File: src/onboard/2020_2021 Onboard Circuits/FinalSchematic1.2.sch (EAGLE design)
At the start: 79 parts, among them IC1 MIC2937A-5.0BT, IC3 A5975D

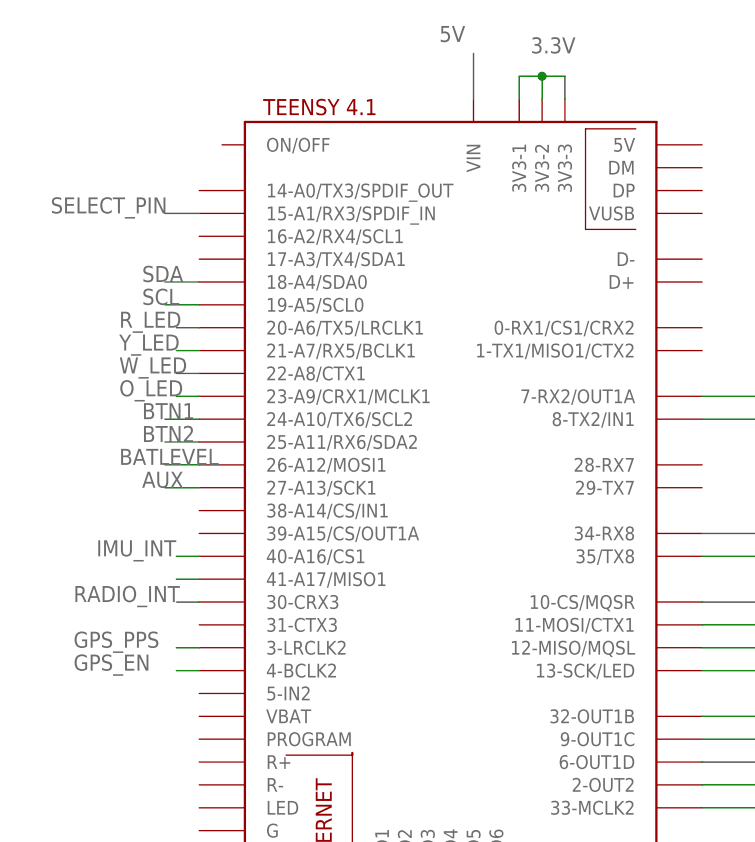
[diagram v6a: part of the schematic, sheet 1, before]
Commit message: Formatting changes and 6v test point
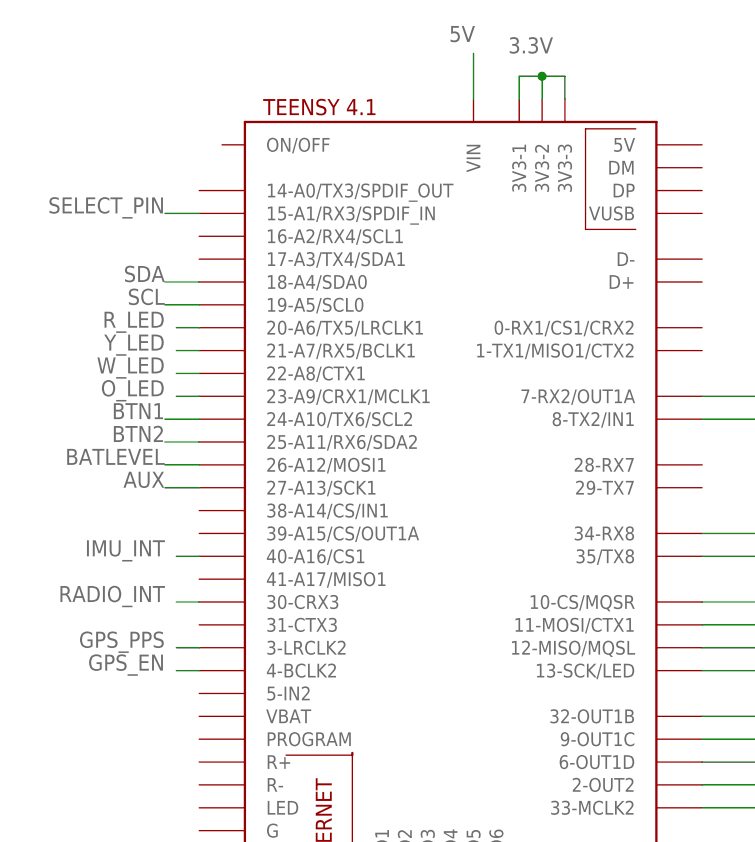
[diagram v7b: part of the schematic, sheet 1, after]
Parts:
- renumbered JUMPER_TO_NAV to NAV
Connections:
- removed net MISO1: TEENSY4.1.41-A17/MISO1
- removed net N$5: TP5.TP
- net 6V: now also TP5.TP
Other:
- note added: "I2C pull-up resistors"
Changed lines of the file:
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@@
 <part name="GND6" library="supply1" library_urn="urn:adsk.eagle:library:371" deviceset="GND" device=""/>
 <part name="L2" library="rcl" library_urn="urn:adsk.eagle:library:334" deviceset="L-US" device="TFI0307" package3d_urn="urn:adsk.eagle:package:23534/1" value="27uH"/>
-<part name="JUMPER_TO_NAV" library="pinhead" library_urn="urn:adsk.eagle:library:325" deviceset="PINHD-1X4" device="" package3d_urn="urn:adsk.eagle:package:22407/2"/>
+<part name="NAV" library="pinhead" library_urn="urn:adsk.eagle:library:325" deviceset="PINHD-1X4" device="" package3d_urn="urn:adsk.eagle:package:22407/2"/>
 <part name="ORANGE" library="adafruit" library_urn="urn:adsk.eagle:library:420" deviceset="R-US_" device="0204/7" package3d_urn="urn:adsk.eagle:package:6240596/1" value="150"/>
 <part name="C3" library="capacitor-wima" library_urn="urn:adsk.eagle:library:116" deviceset="C" device="2,5-3" package3d_urn="urn:adsk.eagle:package:5436/1" value="10uF"/>
@@
 <part name="AUX" library="pinhead" library_urn="urn:adsk.eagle:library:325" deviceset="PINHD-1X3" device="" package3d_urn="urn:adsk.eagle:package:22458/2"/>
 <part name="GND12" library="supply1" library_urn="urn:adsk.eagle:library:371" deviceset="GND" device=""/>
+<part name="GND15" library="supply1" library_urn="urn:adsk.eagle:library:371" deviceset="GND" device=""/>
 </parts>
 <sheets>
@@
 <pinref part="TEENSY4.1" gate="G$1" pin="VIN"/>
 <wire x1="64.77" y1="91.44" x2="64.77" y2="96.52" width="0.1524" layer="91"/>
-<label x="60.96" y="97.79" size="1.778" layer="95"/>
+<label x="63.5" y="97.79" size="1.778" layer="95" align="bottom-center"/>
 </segment>
 </net>
@@
 <wire x1="74.93" y1="93.98" x2="72.39" y2="93.98" width="0.1524" layer="91"/>
 <junction x="72.39" y="93.98"/>
-<label x="71.12" y="96.52" size="1.778" layer="95"/>
+<label x="71.12" y="96.52" size="1.778" layer="95" align="bottom-center"/>
 </segment>
 </net>
@@
 <pinref part="TEENSY4.1" gate="G$1" pin="18-A4/SDA0"/>
 <wire x1="34.29" y1="71.12" x2="30.48" y2="71.12" width="0.1524" layer="91"/>
-<label x="27.94" y="71.12" size="1.778" layer="95"/>
+<label x="30.48" y="71.12" size="1.778" layer="95" align="bottom-right"/>
 </segment>
 </net>
@@
 <pinref part="TEENSY4.1" gate="G$1" pin="19-A5/SCL0"/>
 <wire x1="34.29" y1="68.58" x2="30.48" y2="68.58" width="0.1524" layer="91"/>
-<label x="27.94" y="68.58" size="1.778" layer="95"/>
-</segment>
-</net>
-<net name="MISO1" class="0">
-<segment>
-<pinref part="TEENSY4.1" gate="G$1" pin="41-A17/MISO1"/>
-<wire x1="34.29" y1="38.1" x2="31.75" y2="38.1" width="0.1524" layer="91"/>
+<label x="30.48" y="68.58" size="1.778" layer="95" align="bottom-right"/>
 </segment>
 </net>
@@
 <pinref part="TEENSY4.1" gate="G$1" pin="4-BCLK2"/>
 <wire x1="34.29" y1="27.94" x2="31.75" y2="27.94" width="0.1524" layer="91"/>
-<label x="20.32" y="27.94" size="1.778" layer="95"/>
+<label x="30.48" y="27.94" size="1.778" layer="95" align="bottom-right"/>
 </segment>
 </net>
@@
 <pinref part="TEENSY4.1" gate="G$1" pin="3-LRCLK2"/>
 <wire x1="34.29" y1="30.48" x2="31.75" y2="30.48" width="0.1524" layer="91"/>
-<label x="20.32" y="30.48" size="1.778" layer="95"/>
+<label x="30.48" y="30.48" size="1.778" layer="95" align="bottom-right"/>
 </segment>
 </net>
@@
 <pinref part="TEENSY4.1" gate="G$1" pin="30-CRX3"/>
 <wire x1="34.29" y1="35.56" x2="31.75" y2="35.56" width="0.1524" layer="91"/>
-<label x="20.32" y="35.56" size="1.778" layer="95"/>
+<label x="30.48" y="35.56" size="1.778" layer="95" align="bottom-right"/>
 </segment>
 </net>
@@
 <pinref part="TEENSY4.1" gate="G$1" pin="40-A16/CS1"/>
 <wire x1="34.29" y1="40.64" x2="31.75" y2="40.64" width="0.1524" layer="91"/>
-<label x="22.86" y="40.64" size="1.778" layer="95"/>
+<label x="30.48" y="40.64" size="1.778" layer="95" align="bottom-right"/>
 </segment>
 </net>
@@
 <pinref part="TEENSY4.1" gate="G$1" pin="22-A8/CTX1"/>
 <wire x1="34.29" y1="60.96" x2="31.75" y2="60.96" width="0.1524" layer="91"/>
-<label x="25.4" y="60.96" size="1.778" layer="95"/>
+<label x="30.48" y="60.96" size="1.778" layer="95" align="bottom-right"/>
 </segment>
 </net>
@@
 <pinref part="TEENSY4.1" gate="G$1" pin="21-A7/RX5/BCLK1"/>
 <wire x1="34.29" y1="63.5" x2="31.75" y2="63.5" width="0.1524" layer="91"/>
-<label x="25.4" y="63.5" size="1.778" layer="95"/>
+<label x="30.48" y="63.5" size="1.778" layer="95" align="bottom-right"/>
 </segment>
 </net>
@@
 <pinref part="TEENSY4.1" gate="G$1" pin="20-A6/TX5/LRCLK1"/>
 <wire x1="34.29" y1="66.04" x2="31.75" y2="66.04" width="0.1524" layer="91"/>
-<label x="25.4" y="66.04" size="1.778" layer="95"/>
+<label x="30.48" y="66.04" size="1.778" layer="95" align="bottom-right"/>
 </segment>
 </net>
@@
 <pinref part="TEENSY4.1" gate="G$1" pin="15-A1/RX3/SPDIF_IN"/>
 <wire x1="34.29" y1="78.74" x2="30.48" y2="78.74" width="0.1524" layer="91"/>
-<label x="17.78" y="78.74" size="1.778" layer="95"/>
+<label x="30.48" y="78.74" size="1.778" layer="95" align="bottom-right"/>
 </segment>
 </net>
@@
 <pinref part="TEENSY4.1" gate="G$1" pin="23-A9/CRX1/MCLK1"/>
 <wire x1="34.29" y1="58.42" x2="31.75" y2="58.42" width="0.1524" layer="91"/>
-<label x="25.4" y="58.42" size="1.778" layer="95"/>
+<label x="30.48" y="58.42" size="1.778" layer="95" align="bottom-right"/>
 </segment>
 </net>
@@
 <pinref part="TEENSY4.1" gate="G$1" pin="25-A11/RX6/SDA2"/>
 <wire x1="34.29" y1="53.34" x2="30.48" y2="53.34" width="0.1524" layer="91"/>
-<label x="27.94" y="53.34" size="1.778" layer="95"/>
+<label x="30.48" y="53.34" size="1.778" layer="95" align="bottom-right"/>
 </segment>
 </net>
@@
 <pinref part="TEENSY4.1" gate="G$1" pin="24-A10/TX6/SCL2"/>
 <wire x1="34.29" y1="55.88" x2="30.48" y2="55.88" width="0.1524" layer="91"/>
-<label x="27.94" y="55.88" size="1.778" layer="95"/>
+<label x="30.48" y="55.88" size="1.778" layer="95" align="bottom-right"/>
 </segment>
 </net>
@@
 <pinref part="TEENSY4.1" gate="G$1" pin="26-A12/MOSI1"/>
 <wire x1="34.29" y1="50.8" x2="30.48" y2="50.8" width="0.1524" layer="91"/>
-<label x="25.4" y="50.8" size="1.778" layer="95"/>
+<label x="30.48" y="50.8" size="1.778" layer="95" align="bottom-right"/>
 </segment>
 </net>
@@
 <pinref part="TEENSY4.1" gate="G$1" pin="27-A13/SCK1"/>
 <wire x1="34.29" y1="48.26" x2="30.48" y2="48.26" width="0.1524" layer="91"/>
-<label x="27.94" y="48.26" size="1.778" layer="95"/>
+<label x="30.48" y="48.26" size="1.778" layer="95" align="bottom-right"/>
 </segment>
 </net>
@@
 <text x="101.6" y="81.28" size="1.778" layer="91">RADIO</text>
 <text x="43.18" y="81.28" size="1.778" layer="91">GPS</text>
+<text x="71.12" y="17.78" size="1.778" layer="91" align="center">I2C pull-up resistors</text>
 </plain>
 <instances>
@@
 <attribute name="VALUE" x="50.8" y="7.62" size="1.778" layer="96"/>
 </instance>
-<instance part="JUMPER_TO_NAV" gate="A" x="71.12" y="27.94" smashed="yes" rot="R180">
-<attribute name="NAME" x="66.675" y="41.91" size="1.778" layer="95" rot="R270"/>
+<instance part="NAV" gate="A" x="71.12" y="27.94" smashed="yes" rot="R180">
+<attribute name="NAME" x="76.835" y="19.05" size="1.778" layer="95" rot="R180"/>
 <attribute name="VALUE" x="77.47" y="35.56" size="1.778" layer="96" rot="R180"/>
 </instance>
@@
 <instance part="GND12" gate="1" x="81.28" y="55.88" smashed="yes">
 <attribute name="VALUE" x="78.74" y="53.34" size="1.778" layer="96"/>
+</instance>
+<instance part="GND15" gate="1" x="81.28" y="20.32" smashed="yes">
+<attribute name="VALUE" x="78.74" y="17.78" size="1.778" layer="96"/>
 </instance>
 </instances>
@@
 </segment>
 <segment>
-<pinref part="JUMPER_TO_NAV" gate="A" pin="1"/>
-<wire x1="73.66" y1="22.86" x2="83.82" y2="22.86" width="0.1524" layer="91"/>
-<label x="86.36" y="22.86" size="1.778" layer="95" rot="R180"/>
+<pinref part="NAV" gate="A" pin="1"/>
+<wire x1="73.66" y1="22.86" x2="81.28" y2="22.86" width="0.1524" layer="91"/>
+<pinref part="GND15" gate="1" pin="GND"/>
 </segment>
 <segment>
@@
 <net name="SDA" class="0">
 <segment>
-<pinref part="JUMPER_TO_NAV" gate="A" pin="3"/>
+<pinref part="NAV" gate="A" pin="3"/>
 <wire x1="73.66" y1="27.94" x2="83.82" y2="27.94" width="0.1524" layer="91"/>
 <label x="88.9" y="27.94" size="1.778" layer="95" rot="R180"/>
@@
 <net name="SCL" class="0">
 <segment>
-<pinref part="JUMPER_TO_NAV" gate="A" pin="4"/>
+<pinref part="NAV" gate="A" pin="4"/>
 <wire x1="73.66" y1="30.48" x2="83.82" y2="30.48" width="0.1524" layer="91"/>
 <label x="88.9" y="30.48" size="1.778" layer="95" rot="R180"/>
@@
 <net name="SELECT_PIN" class="0">
 <segment>
-<pinref part="JUMPER_TO_NAV" gate="A" pin="2"/>
+<pinref part="NAV" gate="A" pin="2"/>
 <wire x1="73.66" y1="25.4" x2="91.44" y2="25.4" width="0.1524" layer="91"/>
 <label x="109.22" y="25.4" size="1.778" layer="95" rot="R180"/>
@@
 </segment>
 </net>
-<net name="N$5" class="0">
+<net name="6V" class="0">
 <segment>
 <pinref part="TP5" gate="G$1" pin="TP"/>
 <wire x1="15.24" y1="71.12" x2="17.78" y2="71.12" width="0.1524" layer="91"/>
+<label x="17.78" y="71.12" size="1.778" layer="95"/>
 </segment>
 </net>
@@
 for full support of SPICE simulation.
 </note>
+<note version="9.0" severity="warning">
+Since Version 9.0, EAGLE supports the align property for labels.
+Labels in schematic will not be understood with this version. Update EAGLE to the latest version
+for full support of labels.
+</note>
 </compatibility>
